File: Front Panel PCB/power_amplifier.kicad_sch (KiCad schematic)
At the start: 0 parts

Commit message: Power Supplies Schematic Designed
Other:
- company: (none) -> University of Stellenbosch
- title: (none) -> Output Stage
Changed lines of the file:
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@@
 	(generator_version "10.0")
 	(paper "A4")
+	(title_block
+		(title "Output Stage")
+		(date "2026-06-02")
+		(rev "Rev A")
+		(company "University of Stellenbosch")
+		(comment 1 "Author: Karl Johan Hofmeyr")
+		(comment 2 "Skripsie Project")
+		(comment 3 "BEng - Mechatronic (4th Year)")
+	)
 	(sheet_instances
 		(path "/"

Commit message: Output Stage Schematic Created and complete. Next: Integrate STM32
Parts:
- added C28, C39: 4.7u, symbol Device:C_Polarized
- added C29, C31, C40, C42: 100p, symbol Device:C
- added C30, C32, C36, C38, C41, C43, C48, C49: 100u, symbol Device:C_Polarized
- added C33, C44: C, symbol Device:C
- added C34, C35, C37, C45, C46, C47: 100n, symbol Device:C
- added Q1, Q11, Q13, Q14, Q16, Q2, Q4, Q6: BC546, Package_TO_SOT_THT:TO-92_Inline, symbol Transistor_BJT:BC546
- added Q10, Q19: TIP42, Package_TO_SOT_THT:TO-220-3_Vertical, symbol Transistor_BJT:TIP42
- added Q12, Q3: Q_Dual_NPN_C2C1E1E2, symbol Transistor_BJT:Q_Dual_NPN_C2C1E1E2
- added Q15, Q18, Q5, Q7: BD140, Package_TO_SOT_THT:TO-126-3_Vertical, symbol Transistor_BJT:BD140
- added Q17, Q9: BD139, Package_TO_SOT_THT:TO-126-3_Vertical, symbol Transistor_BJT:BD139
- added Q20, Q8: TIP35, Package_TO_SOT_THT:TO-220-3_Vertical, symbol Transistor_BJT:TIP41
- added R17, R19, R22, R32, R34, R39: 1k, symbol Device:R
- added R18, R23, R33, R38: 22k, symbol Device:R
- added R20, R35: 27k, symbol Device:R
- added R21, R37: 1.8k, symbol Device:R
- added R24, R36: 560, symbol Device:R
- added R25, R26, R40, R41: 3.3k, symbol Device:R
- added R27, R30, R42, R43: 270, symbol Device:R
- added R28, R29, R44, R45: .33, symbol Device:R
- added R31, R46: 10, symbol Device:R
- added RV1, RV2: 1k, symbol Device:R_Potentiometer
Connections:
- new net: C33.1, Q7.2 (C), Q8.1 (B), R27.2
- new net: Q7.1 (E), Q8.2 (C), R28.1
- new net: C30.2, R21.1
- new net: C34.2, R31.1
- new net: C31.1, Q5.2 (C), Q6.1 (C), Q9.3 (B), R22.2
- new net: C31.2, Q1.1 (C), Q5.3 (B), R24.1
- new net: C39.2, R32.1
- new net: C40.2, R32.2, R33.2, R34.2
- new net: Q2.2 (B), R21.2, R23.2
- new net: Q1.3 (E), Q2.3 (E), Q4.1 (C)
- new net: C46.2, R46.1
- new net: C42.1, Q15.2 (C), Q16.1 (C), Q17.3 (B), R39.2
- new net: C42.2, Q11.1 (C), Q15.3 (B), R36.1
- new net: Q11.2 (B), R34.1
- new net: Q11.3 (E), Q13.1 (C), Q14.3 (E)
- new net: C29.2, R17.2, R18.2, R19.2
- new net: Q10.2 (C), Q9.1 (E), R29.2
- new net: Q10.1 (B), Q9.2 (C), R30.1
- new net: C33.2, Q6.3 (E), Q7.3 (B), R25.2, RV1.3
- new net: Q1.2 (B), R19.1
- new net: Q14.2 (B), R37.2, R38.2
- new net: Q12.2 (C1), Q13.2 (B), R35.1
- new net: Q12.1 (C2), Q13.3 (E)
- new net: C41.2, R37.1
- new net: Q16.2 (B), R39.1, RV2.1, RV2.2
- new net: C44.2, Q16.3 (E), Q18.3 (B), R40.2, RV2.3
- new net: Q17.1 (E), Q19.2 (C), R44.2
- new net: C28.2, R17.1
- new net: Q6.2 (B), R22.1, RV1.1, RV1.2
- new net: Q17.2 (C), Q19.1 (B), R42.1
- new net: C32.2, R25.1, R26.2
- new net: C43.2, R40.1, R41.2
- new net: Q3.2 (C1), Q4.2 (B), R20.1
- new net: Q3.1 (C2), Q4.3 (E)
- new net: Q18.1 (E), Q20.2 (C), R45.1
- new net: C44.1, Q18.2 (C), Q20.1 (B), R43.2
- new net GND: C29.1, C30.1, C34.1, C35.2, C36.1, C37.1, C38.2, C40.1, C41.1, C45.1, C46.1, C47.2, C48.2, C49.1, R18.1, R33.1
- new net In+: C28.1
- new net In-: C39.1
- new net Out+: C32.1, R23.1, R28.2, R29.1, R31.2
- new net Out-: C43.1, R38.1, R44.1, R45.2, R46.2
- new net VCC: C37.2, C38.1, C45.2, C48.1, Q10.3 (E), Q14.1 (C), Q15.1 (E), Q19.3 (E), Q2.1 (C), Q5.1 (E), R20.2, R24.2, R30.2, R35.2, R36.2, R42.2
- new net VEE: C35.1, C36.2, C47.1, C49.2, Q12.3 (E1), Q12.4 (E2), Q20.3 (E), Q3.3 (E1), Q3.4 (E2), Q8.3 (E), R26.1, R27.1, R41.1, R43.1
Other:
- note added: "A"
- note added: "B"

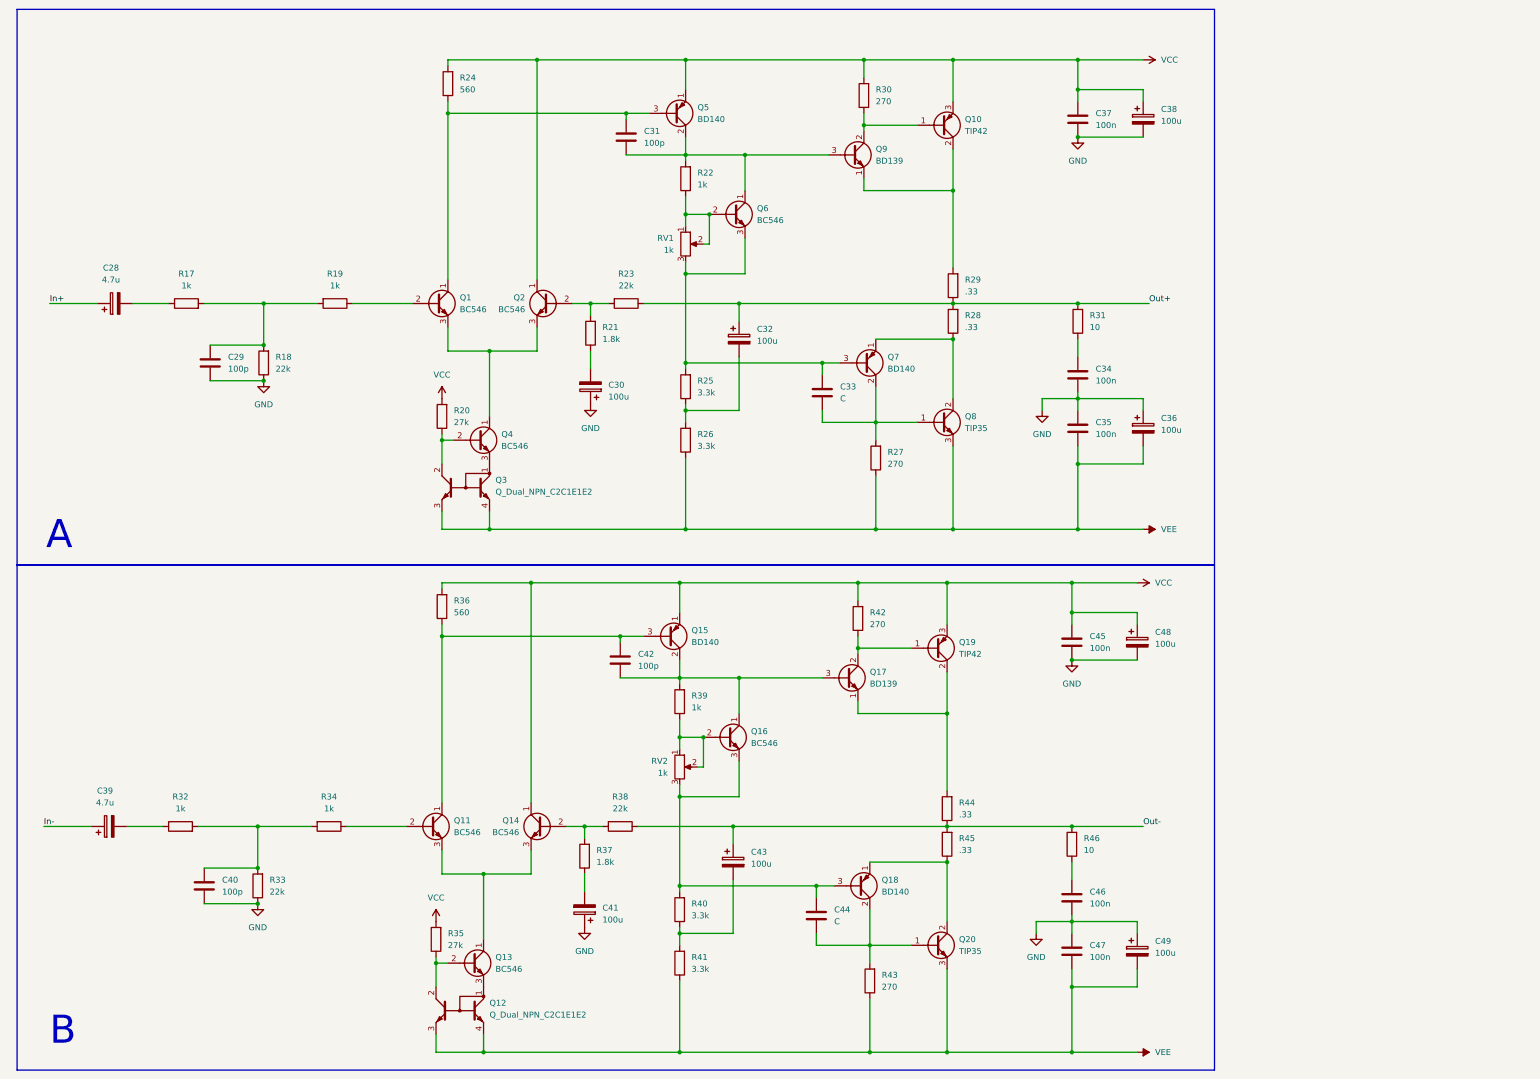
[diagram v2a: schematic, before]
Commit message: Bill of materials ETC finalised, selecting footprints next
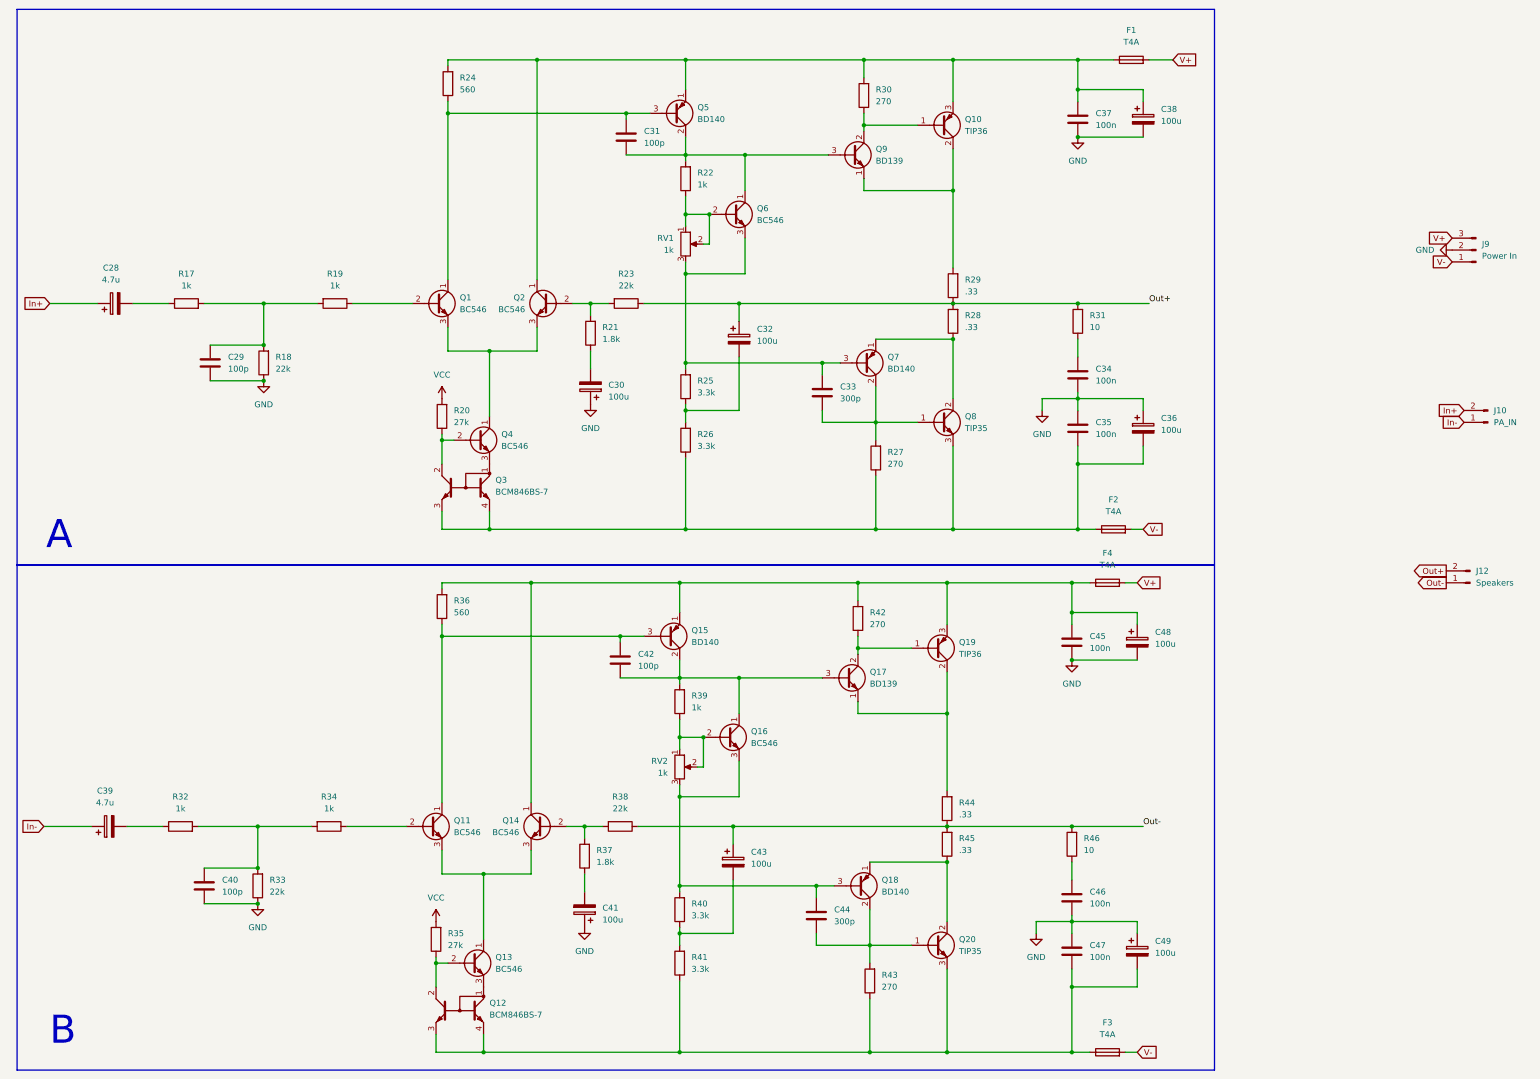
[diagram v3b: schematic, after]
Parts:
- added F1, F2, F3, F4: T4A, symbol Device:Fuse
- added J10: PA_IN, symbol Connector:Conn_01x02_Pin
- added J12: Speakers, symbol Connector:Conn_01x02_Pin
- added J9: Power In, symbol Connector:Conn_01x03_Pin
- C33, C44: value C -> 300p
- Q10, Q19: value TIP42 -> TIP36
- Q12, Q3: value Q_Dual_NPN_C2C1E1E2 -> BCM846BS-7
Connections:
- net GND: now also J9.2 (Pin_2)
- net In+: now also J10.2 (Pin_2)
- net In-: now also J10.1 (Pin_1)
- net Out+: now also J12.2 (Pin_2)
- net Out-: now also J12.1 (Pin_1)
- net VCC: no longer C37.2, C38.1, C45.2, C48.1, Q10.3 (E), Q14.1 (C), Q15.1 (E), Q19.3 (E), Q2.1 (C), Q5.1 (E), R24.2, R30.2, R36.2, R42.2
- net VEE: no longer names the net of C35.1, C36.2, Q3.3 (E1), Q3.4 (E2), Q8.3 (E), R26.1, R27.1
- net VEE: now also F2.1; no longer C47.1, C49.2, Q12.3 (E1), Q12.4 (E2), Q20.3 (E), R41.1, R43.1
- new net: C47.1, C49.2, F3.1, Q12.3 (E1), Q12.4 (E2), Q20.3 (E), R41.1, R43.1
- new net: C37.2, C38.1, F1.1, Q10.3 (E), Q2.1 (C), Q5.1 (E), R24.2, R30.2
- new net: C45.2, C48.1, F4.1, Q14.1 (C), Q15.1 (E), Q19.3 (E), R36.2, R42.2
- new net V+: F1.2, F4.2, J9.3 (Pin_3)
- new net V-: F2.2, F3.2, J9.1 (Pin_1)
